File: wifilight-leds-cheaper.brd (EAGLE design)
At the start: 50.8 x 50.8 mm, 50 parts, among them Q1 BUK98180-100A, Q2 BUK98180-100A, Q3 BUK98180-100A, Q4 BUK98180-100A, U2 PCA9685

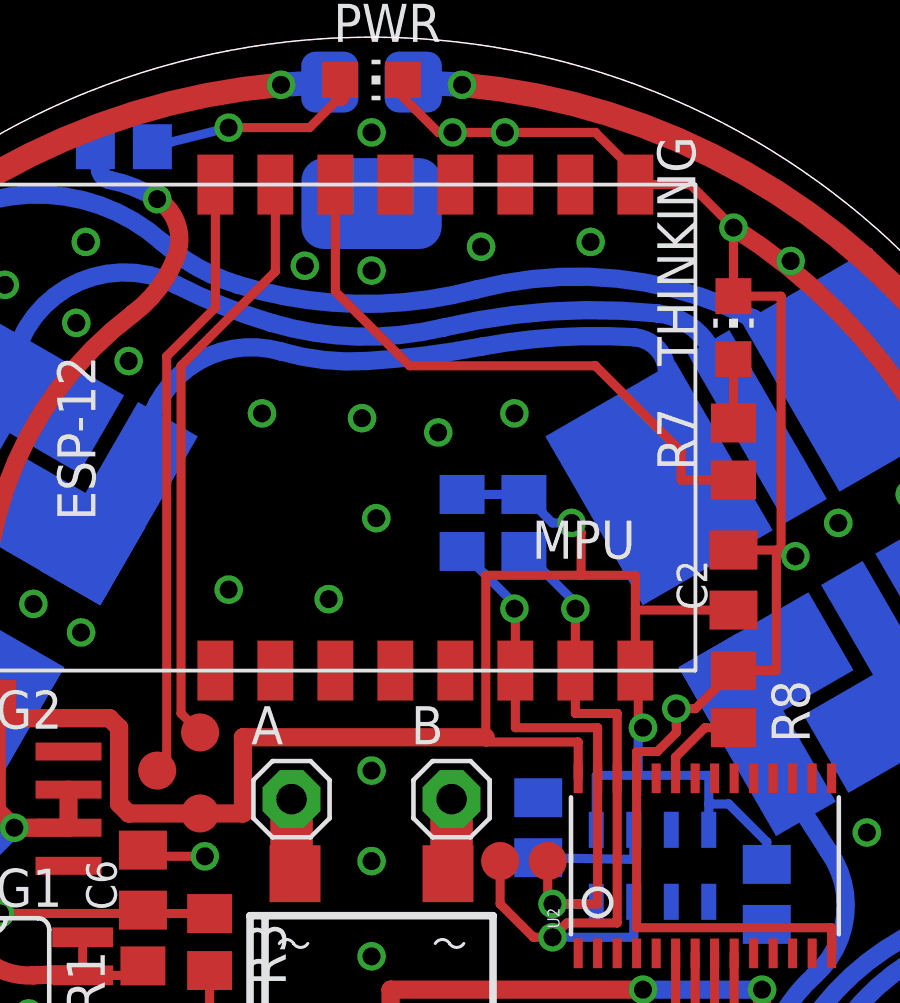
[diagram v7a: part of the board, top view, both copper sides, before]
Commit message: add TXD, RXD & GPIO0 pins pogopins for programming
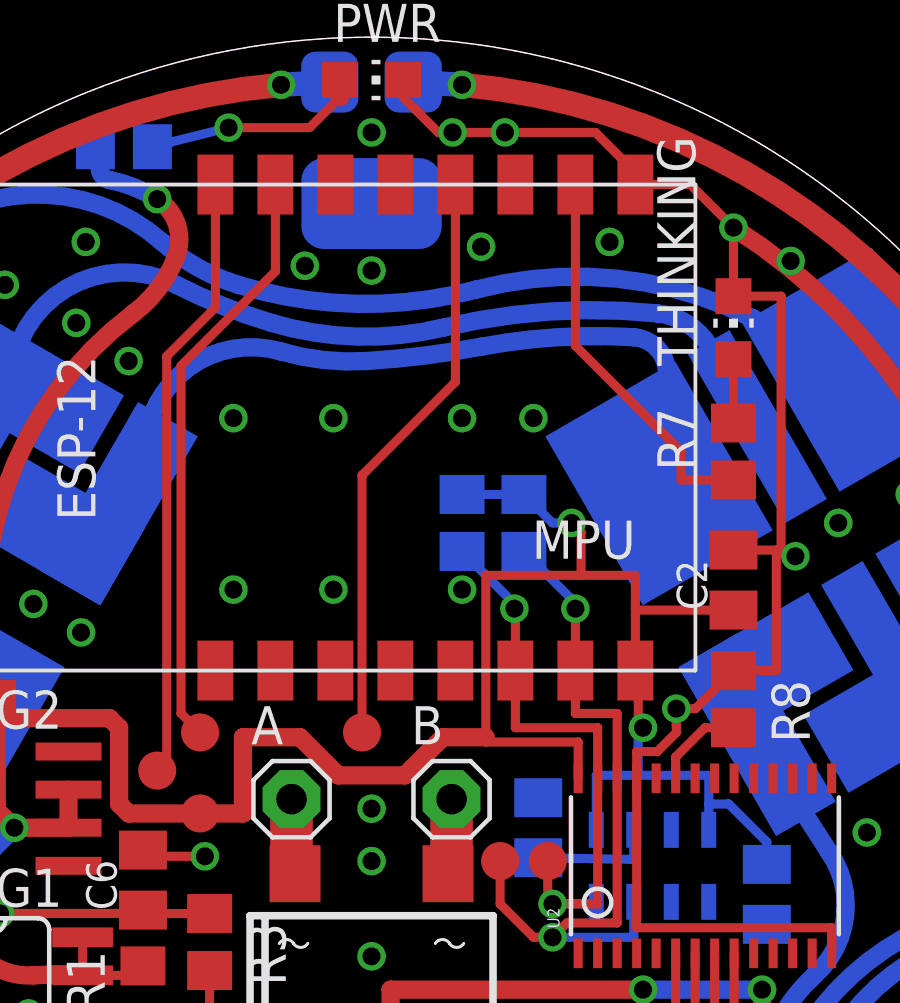
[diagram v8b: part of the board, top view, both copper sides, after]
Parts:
- added TPGPIO0: TEST-POINT3X5, SparkFun-Passives:PAD.03X.05
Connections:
- removed net N$33: MPU.4
- removed net N$35: MPU.2
- new net DISCO: MPU.6
- new net GPIO0: MPU.4, TPGPIO0.P$1
- net THINKING: now also MPU.2; no longer MPU.6
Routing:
- net GPIO0: track 0.00 -> 19.6 mm
- net THINKING: track 20.0 -> 13.1 mm
- net 3.3V: track 101.4 -> 102.4 mm
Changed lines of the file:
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@@
 <element name="TPTX" library="SparkFun-Passives" package="PAD.03X.05" value="TEST-POINT3X5" x="18.25625" y="26.3525"/>
 <element name="TPRX" library="SparkFun-Passives" package="PAD.03X.05" value="TEST-POINT3X5" x="19.685" y="27.6225"/>
+<element name="TPGPIO0" library="SparkFun-Passives" package="PAD.03X.05" value="TEST-POINT3X5" x="25.0825" y="27.6225"/>
 </elements>
 <signals>
@@
 <via x="29.845" y="47.625" extent="1-16" drill="0.6"/>
 <via x="17.30375" y="40.005" extent="1-16" drill="0.6"/>
-<via x="21.74875" y="38.25875" extent="1-16" drill="0.6"/>
-<via x="23.97125" y="32.0675" extent="1-16" drill="0.6"/>
-<via x="25.55875" y="34.76625" extent="1-16" drill="0.6"/>
-<via x="25.0825" y="38.1" extent="1-16" drill="0.6"/>
-<via x="27.6225" y="37.62375" extent="1-16" drill="0.6"/>
-<via x="30.1625" y="38.25875" extent="1-16" drill="0.6"/>
+<via x="20.79625" y="38.1" extent="1-16" drill="0.6"/>
+<via x="24.13" y="32.385" extent="1-16" drill="0.6"/>
+<via x="28.41625" y="32.385" extent="1-16" drill="0.6"/>
+<via x="24.13" y="38.1" extent="1-16" drill="0.6"/>
+<via x="28.41625" y="38.1" extent="1-16" drill="0.6"/>
+<via x="30.7975" y="38.1" extent="1-16" drill="0.6"/>
 <via x="25.4" y="47.625" extent="1-16" drill="0.6"/>
-<via x="20.6375" y="32.385" extent="1-16" drill="0.6"/>
+<via x="20.79625" y="32.385" extent="1-16" drill="0.6"/>
 <via x="7.62" y="12.065" extent="1-16" drill="0.6"/>
 <via x="11.7475" y="12.7" extent="1-16" drill="0.6"/>
@@
 <via x="25.4" y="43.02125" extent="1-16" drill="0.6"/>
 <via x="29.05125" y="43.815" extent="1-16" drill="0.6"/>
-<via x="32.7025" y="43.97375" extent="1-16" drill="0.6"/>
+<via x="33.3375" y="43.97375" extent="1-16" drill="0.6"/>
 <via x="25.4" y="10.795" extent="1-16" drill="0.6"/>
 <via x="34.13125" y="6.50875" extent="1-16" drill="0.6"/>
@@
 <via x="34.44875" y="2.8575" extent="1-16" drill="0.6"/>
 <via x="39.0525" y="5.55625" extent="1-16" drill="0.6"/>
-<via x="25.4" y="26.3525" extent="1-16" drill="0.6"/>
+<via x="25.4" y="25.0825" extent="1-16" drill="0.6"/>
 <via x="25.4" y="23.33625" extent="1-16" drill="0.6"/>
 <via x="25.4" y="20.16125" extent="1-16" drill="0.6"/>
@@
 <wire x1="32.0675" y1="34.6075" x2="31.43" y2="34.6075" width="0.3048" layer="16"/>
 <wire x1="31.43" y1="34.6075" x2="30.48" y2="35.5575" width="0.3048" layer="16"/>
-<wire x1="29.21" y1="27.46375" x2="21.11375" y2="27.46375" width="0.6096" layer="1"/>
 <wire x1="21.11375" y1="27.46375" x2="21.11375" y2="24.92375" width="0.6096" layer="1"/>
 <wire x1="21.11375" y1="24.92375" x2="19.685" y2="24.92375" width="0.6096" layer="1"/>
@@
 <wire x1="17.4625" y1="41.5925" x2="12.90625" y2="28.575" width="0.6096" layer="1" curve="67.571913"/>
 <contactref element="TP3.3V" pad="P$1"/>
+<wire x1="21.11375" y1="27.46375" x2="23.01875" y2="27.46375" width="0.6096" layer="1"/>
+<wire x1="23.01875" y1="27.46375" x2="24.28875" y2="26.19375" width="0.6096" layer="1"/>
+<wire x1="24.28875" y1="26.19375" x2="26.51125" y2="26.19375" width="0.6096" layer="1"/>
+<wire x1="26.51125" y1="26.19375" x2="27.78125" y2="27.46375" width="0.6096" layer="1"/>
+<wire x1="27.78125" y1="27.46375" x2="29.21" y2="27.46375" width="0.6096" layer="1"/>
 </signal>
 <signal name="N$13">
@@
 <wire x1="35.71875" y1="36.98875" x2="35.71875" y2="36.03875" width="0.3048" layer="1"/>
 <wire x1="35.71875" y1="36.03875" x2="37.465" y2="36.03875" width="0.3048" layer="1"/>
-<contactref element="MPU" pad="6"/>
-<wire x1="24.195" y1="45.88625" x2="24.195" y2="42.32125" width="0.3048" layer="1"/>
-<wire x1="24.195" y1="42.32125" x2="26.67" y2="39.84625" width="0.3048" layer="1"/>
-<wire x1="26.67" y1="39.84625" x2="32.86125" y2="39.84625" width="0.3048" layer="1"/>
-<wire x1="32.86125" y1="39.84625" x2="35.71875" y2="36.98875" width="0.3048" layer="1"/>
+<wire x1="32.195" y1="40.5125" x2="35.71875" y2="36.98875" width="0.3048" layer="1"/>
+<contactref element="MPU" pad="2"/>
+<wire x1="32.195" y1="45.88625" x2="32.195" y2="40.5125" width="0.3048" layer="1"/>
 </signal>
 <signal name="N$19">
@@
 <contactref element="MPU" pad="9"/>
 </signal>
-<signal name="N$33">
+<signal name="GPIO0">
 <contactref element="MPU" pad="4"/>
+<contactref element="TPGPIO0" pad="P$1"/>
+<wire x1="25.0825" y1="27.6225" x2="25.0825" y2="36.195" width="0.3048" layer="1"/>
+<wire x1="25.0825" y1="36.195" x2="28.195" y2="39.3075" width="0.3048" layer="1"/>
+<wire x1="28.195" y1="45.88625" x2="28.195" y2="39.3075" width="0.3048" layer="1"/>
 </signal>
 <signal name="N$34">
 <contactref element="MPU" pad="3"/>
-</signal>
-<signal name="N$35">
-<contactref element="MPU" pad="2"/>
 </signal>
 <signal name="N$36">
@@
 <wire x1="22.195" y1="42.99125" x2="22.195" y2="45.88625" width="0.3048" layer="1"/>
 </signal>
+<signal name="DISCO">
+<contactref element="MPU" pad="6"/>
+</signal>
 </signals>
